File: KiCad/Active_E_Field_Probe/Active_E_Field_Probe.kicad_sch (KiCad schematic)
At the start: 6 parts

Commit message: .
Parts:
- C15: value {0.5*C_s} -> {0.4*C_s}
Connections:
- net Amp_out: now also C15.2, R1.1, X1.1 (D); no longer R1.2, R9.1
- new net vo: R1.2, R9.1
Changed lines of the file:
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@@
+	(wire
+		(pts
+			(xy 116.84 106.68) (xy 116.84 93.98)
+		)
+		(stroke
+			(width 0)
+			(type default)
+		)
+	)
 	(wire
 		(pts
@@
 	(wire
 		(pts
+			(xy 106.68 93.98) (xy 116.84 93.98)
+		)
+		(stroke
+			(width 0)
+			(type default)
+		)
+	)
+	(wire
+		(pts
 			(xy 116.84 120.65) (xy 116.84 127)
 		)
@@
 		)
 	)
-	(global_label "Amp_out"
+	(global_label "vo"
 		(shape output)
 		(at 142.24 106.68 0)
@@
 		)
 		(property "Intersheetrefs" "${INTERSHEET_REFS}"
-			(at 153.1474 106.68 0)
-			(effects
-				(font
-					(size 1.27 1.27)
-				)
-				(justify left)
+			(at 147.3418 106.68 0)
+			(effects
+				(font
+					(size 1.27 1.27)
+				)
+				(justify left)
+				(hide yes)
+			)
+		)
+	)
+	(global_label "Amp_out"
+		(shape output)
+		(at 106.68 93.98 180)
+		(fields_autoplaced yes)
+		(effects
+			(font
+				(size 1.27 1.27)
+			)
+			(justify right)
+		)
+		(property "Intersheetrefs" "${INTERSHEET_REFS}"
+			(at 95.7726 93.98 0)
+			(effects
+				(font
+					(size 1.27 1.27)
+				)
+				(justify right)
 				(hide yes)
 			)
@@
 			)
 		)
-		(property "Value" "{0.5*C_s}"
+		(property "Value" "{0.4*C_s}"
 			(at 104.0737 100.33 90)
 			(show_name yes)

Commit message: 2 stage
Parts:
- removed C14: {C_s}, symbol SLiCAP:C
- removed C15: {0.4*C_s}, symbol SLiCAP:C
- removed R1, R9: 50, symbol SLiCAP:R
- added C22: {C_s}, symbol SLiCAP:C
- added C23: {0.4*C_s}, symbol SLiCAP:C
- added R16, R17: 50, symbol SLiCAP:R
- added X2, X3: ~, symbol SLiCAP:XM
- X1: ID {ID_1} -> {ID1_N}; L {L_1} -> {L1_N}; W {W_1} -> {W1_N}
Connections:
- net 0: now also R17.2, X2.3 (S), X2.4 (B), X3.3 (S), X3.4 (B)
- net Amp_out: now also C23.2, R16.1, X2.1 (D), X3.1 (D); no longer X1.1 (D)
- net vo: now also R16.2, R17.1
- net at X1.2 (G): now also C22.2, C23.1
- net at V1.1 (p): now also C22.1
- new net: X1.1 (D), X2.2 (G), X3.2 (G)

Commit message: something
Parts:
- removed X1: ~, symbol SLiCAP:XM
- added X1: ~, symbol SLiCAP:XMD
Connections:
- net 0: now also X1.4 (G2)
- net at C22.2, C23.1: now also X1.3 (G1)
- net at X2.2 (G), X3.2 (G): now also X1.2 (D2)
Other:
- moved on the sheet: C23, R16, R17, X2, X3

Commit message: NoiseStuff
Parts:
- added X4, X5: ~, symbol SLiCAP:M_noise
- R17: noisetemp {T_op_max} -> {0}
- X1: model CMOS18N -> CMOS18ND
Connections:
- net 0: now also X1.1 (D1), X4.2 (comm), X5.1 (ext), X5.2 (comm); no longer X1.4 (G2)
- net at C22.2, C23.1: now also X4.1 (ext); no longer X1.3 (G1)
- new net: X1.3 (G1), X4.3 (int)
- new net: X1.4 (G2), X5.3 (int)
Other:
- moved on the sheet: C23, R16, R17, V1, X1, X2, X3

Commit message: stuff
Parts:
- added X6: ~, symbol SLiCAP:M_noise
- C23: value {0.4*C_s} -> {0.56*C_s}
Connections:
- net 0: now also X6.2 (comm)
- net at X2.2 (G), X3.2 (G): now also X6.3 (int); no longer X1.2 (D2)
- new net: X1.2 (D2), X6.1 (ext)
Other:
- moved on the sheet: R16, R17, X2, X3

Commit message: CG stage added
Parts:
- removed X6: ~, symbol SLiCAP:M_noise
- added X6, X7: ~, symbol SLiCAP:XM
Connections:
- net 0: now also X6.2 (G), X6.4 (B), X7.1 (D), X7.2 (G), X7.4 (B); no longer X1.1 (D1)
- net at X2.2 (G), X3.2 (G): now also X6.1 (D)
- net at X1.2 (D2): now also X6.3 (S)
- new net: X1.1 (D1), X7.3 (S)
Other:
- moved on the sheet: C22, R16, R17, V1, X1, X2, X3, X4, X5

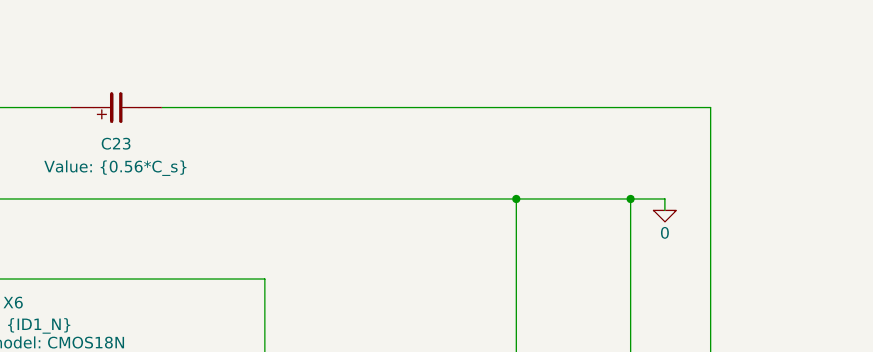
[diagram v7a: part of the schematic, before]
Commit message: cleaned up code and pages
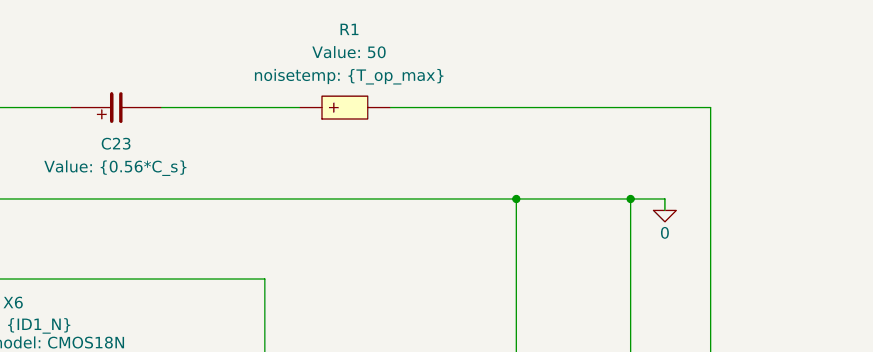
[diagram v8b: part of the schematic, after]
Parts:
- added R1: 50, symbol SLiCAP:R
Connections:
- net Amp_out: now also R1.2; no longer C23.2
- new net: C23.2, R1.1
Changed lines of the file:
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@@
-	(wire
-		(pts
-			(xy 171.45 39.37) (xy 232.41 39.37)
-		)
-		(stroke
-			(width 0)
-			(type default)
-		)
-	)
 	(wire
 		(pts
@@
 	(wire
 		(pts
+			(xy 171.45 39.37) (xy 186.69 39.37)
+		)
+		(stroke
+			(width 0)
+			(type default)
+		)
+	)
+	(wire
+		(pts
 			(xy 210.82 99.06) (xy 214.63 99.06)
 		)
@@
 		(pts
 			(xy 210.82 49.53) (xy 210.82 68.58)
+		)
+		(stroke
+			(width 0)
+			(type default)
+		)
+	)
+	(wire
+		(pts
+			(xy 196.85 39.37) (xy 232.41 39.37)
 		)
 		(stroke
@@
 					(unit 1)
 				)
+			)
+		)
+	)
+	(symbol
+		(lib_id "SLiCAP:R")
+		(at 191.77 39.37 90)
+		(unit 1)
+		(exclude_from_sim no)
+		(in_bom yes)
+		(on_board yes)
+		(dnp no)
+		(property "Reference" "R1"
+			(at 192.278 30.734 90)
+			(effects
+				(font
+					(size 1.27 1.27)
+				)
+			)
+		)
+		(property "Value" "50"
+			(at 192.278 33.274 90)
+			(show_name yes)
+			(effects
+				(font
+					(size 1.27 1.27)
+				)
+			)
+		)
+		(property "Footprint" ""
+			(at 194.945 38.735 0)
+			(effects
+				(font
+					(size 1.27 1.27)
+				)
+				(hide yes)
+			)
+		)
+		(property "Datasheet" ""
+			(at 194.945 38.735 0)
+			(effects
+				(font
+					(size 1.27 1.27)
+				)
+				(hide yes)
+			)
+		)
+		(property "Description" "Resistor (cannot have zero resistance)"
+			(at 197.612 18.288 0)
+			(effects
+				(font
+					(size 1.27 1.27)
+				)
+				(hide yes)
+			)
+		)
+		(property "model" "R"
+			(at 195.58 37.465 0)
+			(show_name yes)
+			(effects
+				(font
+					(size 1.27 1.27)
+				)
+				(justify left)
+				(hide yes)
+			)
+		)
+		(property "noisetemp" "{T_op_max}"
+			(at 192.278 35.814 90)
+			(show_name yes)
+			(effects
+				(font
+					(size 1.27 1.27)
+				)
+			)
+		)
+		(property "noiseflow" "0"
+			(at 191.77 30.48 90)
+			(show_name yes)
+			(effects
+				(font
+					(size 1.27 1.27)
+				)
+				(hide yes)
+			)
+		)
+		(property "dcvar" "0"
+			(at 191.77 33.02 90)
+			(show_name yes)
+			(effects
+				(font
+					(size 1.27 1.27)
+				)
+				(hide yes)
+			)
+		)
+		(property "dcvarlot" "0"
+			(at 191.77 35.56 90)
+			(show_name yes)
+			(effects
+				(font
+					(size 1.27 1.27)
+				)
+				(hide yes)
+			)
+		)
+		(pin "2"
+		)
+		(pin "1"
+		)
+		(instances
+			(project "Active_E_Field_Probe"
+				(path "/8648b04b-5135-4efe-a9b1-6520ac7dc88b"
+					(reference "R1")
+					(unit 1)
+				)
